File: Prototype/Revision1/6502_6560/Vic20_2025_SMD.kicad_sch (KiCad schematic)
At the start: 20 parts

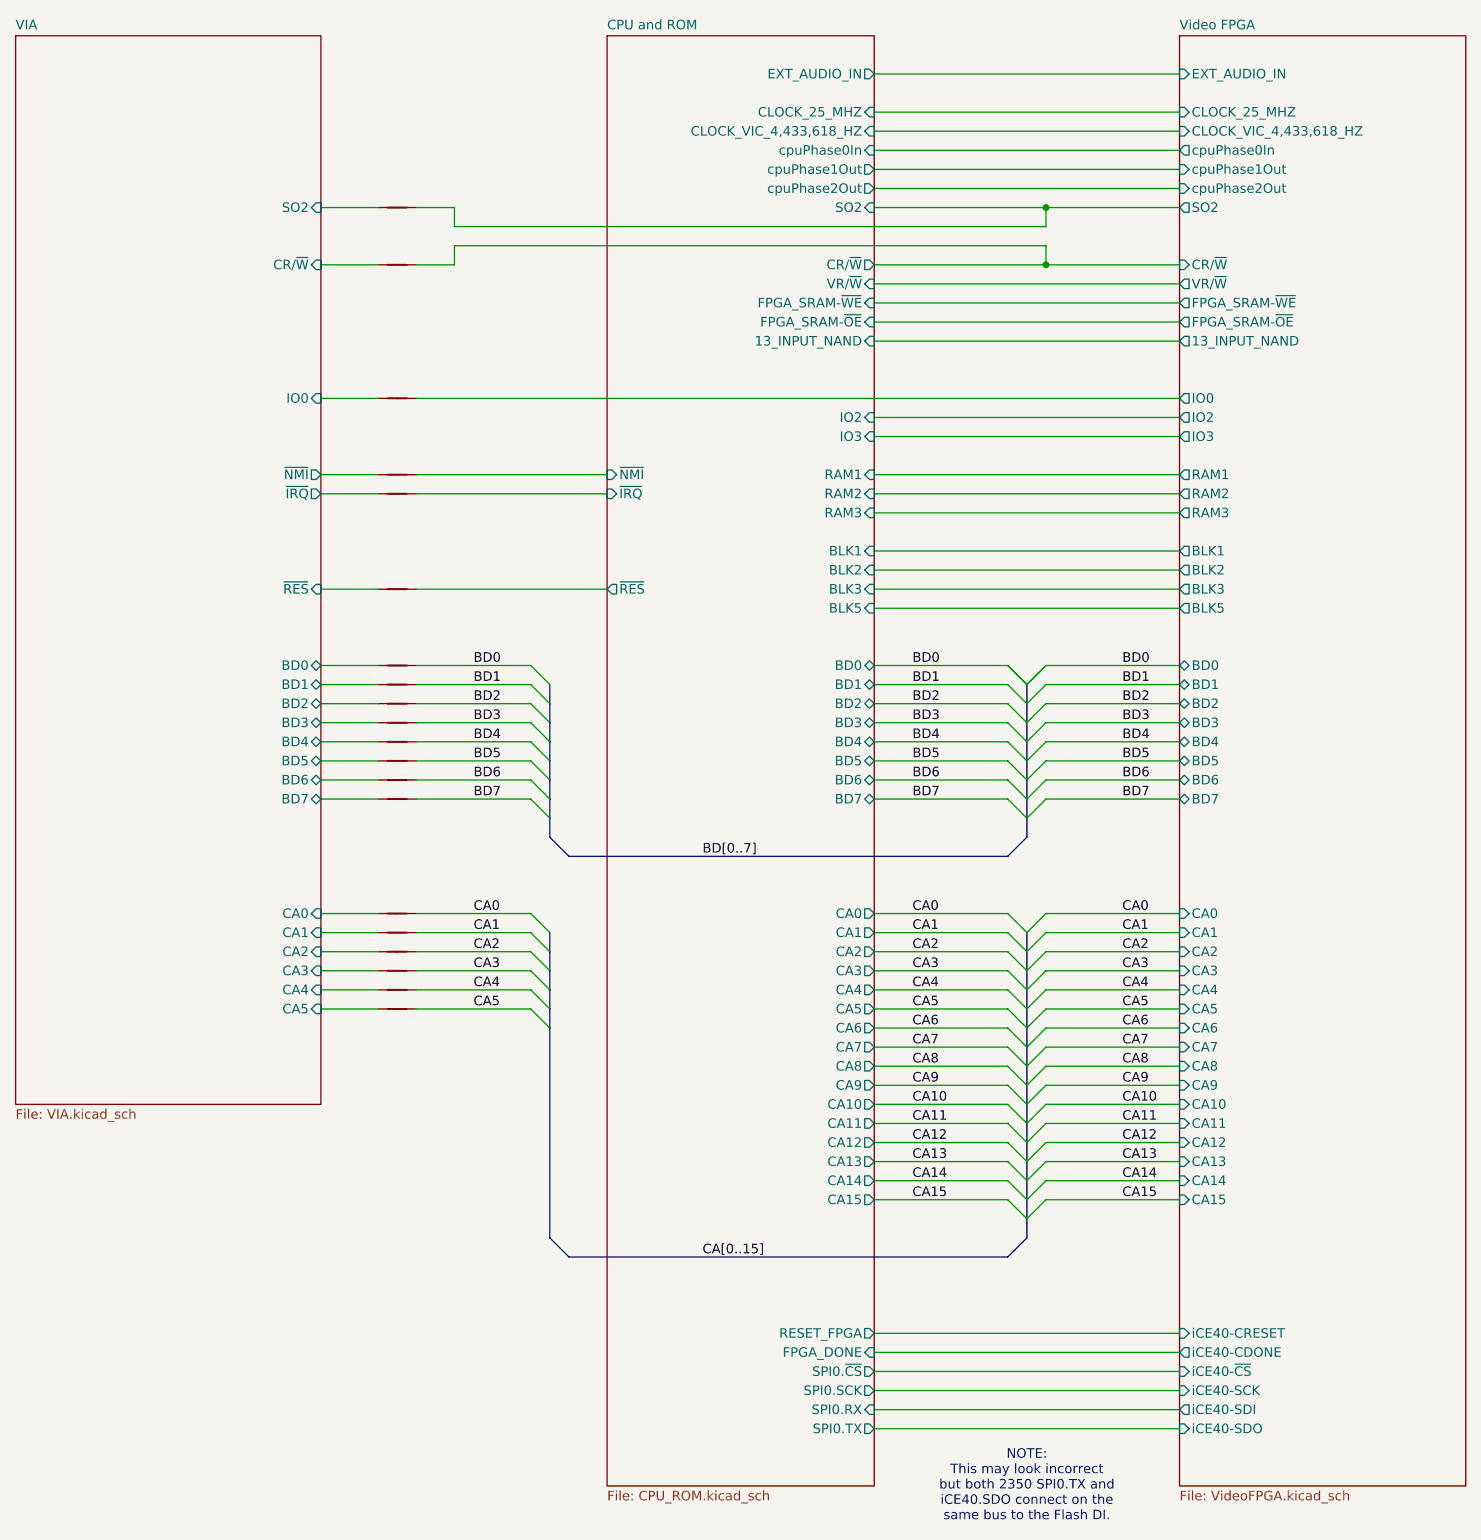
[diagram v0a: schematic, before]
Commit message: - Initial component placement for protype 2, no routing done yet.
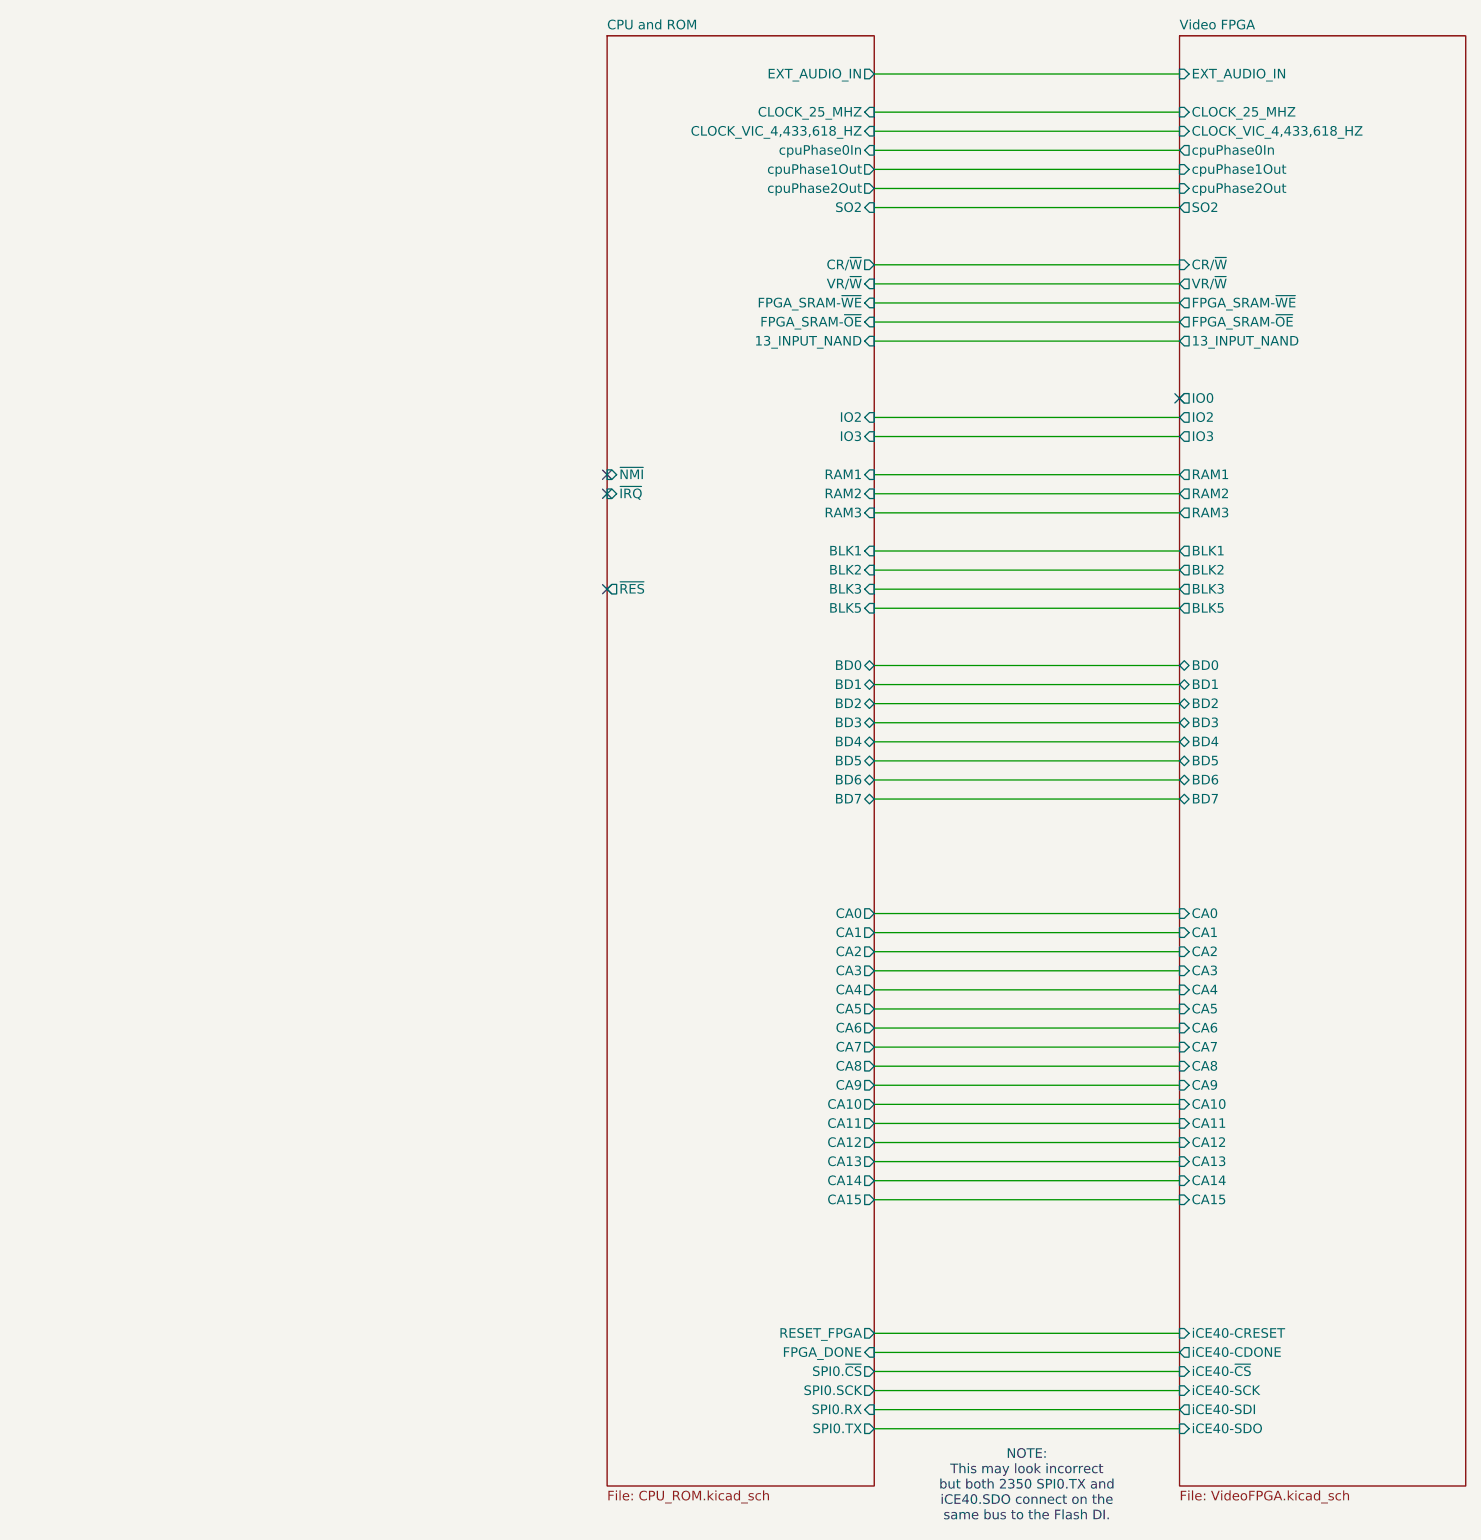
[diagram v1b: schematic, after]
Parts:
- removed NT1, NT10, NT11, NT12, NT13, NT14, NT15, NT16, NT17, NT18, NT19, NT2, NT20, NT3, NT4, NT5, NT6, NT7, NT8, NT9: NetTie_2, symbol Device:NetTie_2
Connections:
- no-connect marks 0 -> 4
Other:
- removed sheet VIA
